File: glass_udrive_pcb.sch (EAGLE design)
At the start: 23 parts

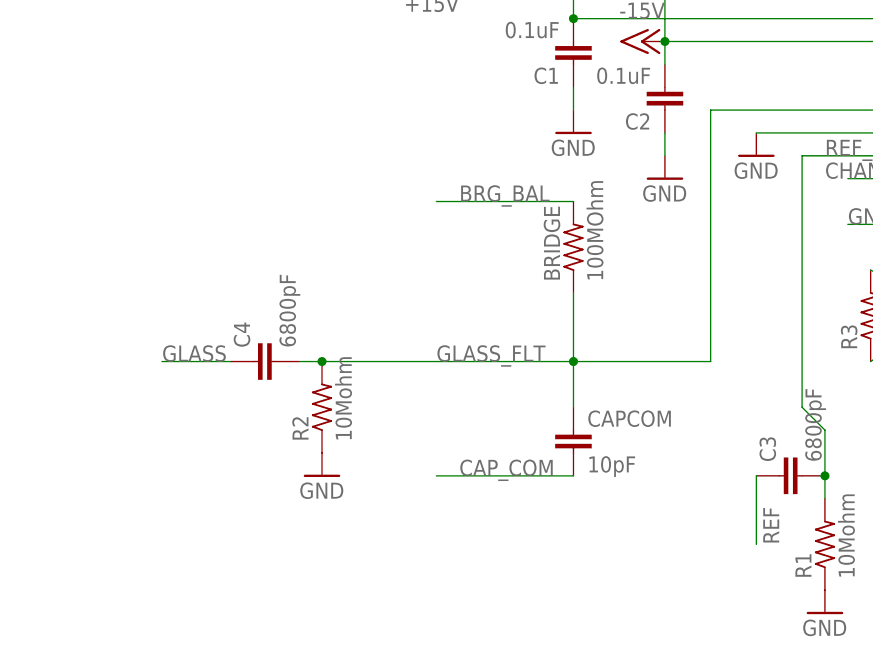
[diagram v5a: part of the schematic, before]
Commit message: solved the order of CAPCOM and Bridge balance nets and routing as per GFL suggestions.
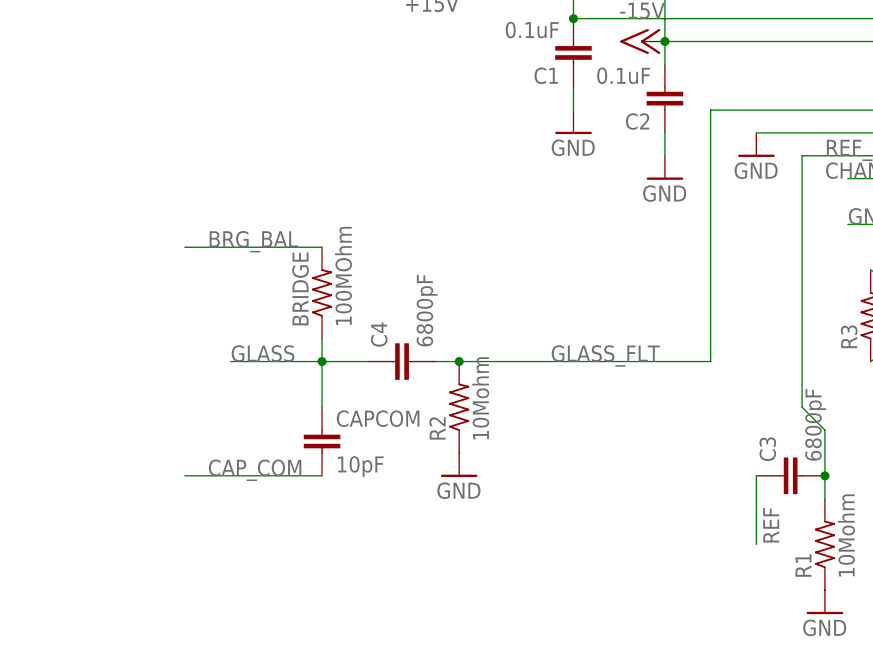
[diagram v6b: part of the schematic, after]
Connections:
- net GLASS: now also BRIDGE.1, CAPCOM.1
- net GLASS_FLT: no longer BRIDGE.1, CAPCOM.1
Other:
- moved on the sheet: BRIDGE, C4, CAPCOM, R2
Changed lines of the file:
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@@
 <instance part="FRAME1" gate="G$2" x="121.92" y="-10.16"/>
 <instance part="OMNETICS" gate="G$1" x="58.42" y="116.84"/>
-<instance part="BRIDGE" gate="R" x="116.84" y="71.12" rot="R90"/>
-<instance part="CAPCOM" gate="C" x="116.84" y="50.8"/>
+<instance part="BRIDGE" gate="R" x="88.9" y="66.04" rot="R90"/>
+<instance part="CAPCOM" gate="C" x="88.9" y="50.8"/>
 <instance part="C1" gate="C" x="116.84" y="91.44" rot="R180"/>
 <instance part="C2" gate="C" x="127" y="86.36" rot="R180"/>
@@
 <instance part="REF" gate="P" x="-5.08" y="15.24"/>
 <instance part="R3" gate="R" x="149.86" y="63.5" rot="R90"/>
-<instance part="R2" gate="R" x="88.9" y="53.34" rot="R90"/>
-<instance part="C4" gate="C" x="81.28" y="58.42" rot="R90"/>
+<instance part="R2" gate="R" x="104.14" y="53.34" rot="R90"/>
+<instance part="C4" gate="C" x="96.52" y="58.42" rot="R90"/>
 <instance part="GND3" gate="1" x="137.16" y="81.28"/>
-<instance part="GND4" gate="1" x="88.9" y="45.72"/>
+<instance part="GND4" gate="1" x="104.14" y="45.72"/>
 <instance part="R1" gate="R" x="144.78" y="38.1" rot="R90"/>
 <instance part="C3" gate="C" x="139.7" y="45.72" rot="R90"/>
@@
 <segment>
 <pinref part="CAPCOM" gate="C" pin="2"/>
-<wire x1="116.84" y1="45.72" x2="101.6" y2="45.72" width="0.1524" layer="91"/>
-<label x="104.14" y="45.72" size="1.778" layer="95"/>
+<wire x1="88.9" y1="45.72" x2="73.66" y2="45.72" width="0.1524" layer="91"/>
+<label x="76.2" y="45.72" size="1.778" layer="95"/>
 </segment>
 </net>
@@
 <segment>
 <pinref part="BRIDGE" gate="R" pin="2"/>
-<wire x1="116.84" y1="76.2" x2="101.6" y2="76.2" width="0.1524" layer="91"/>
-<label x="104.14" y="76.2" size="1.778" layer="95"/>
+<wire x1="88.9" y1="71.12" x2="73.66" y2="71.12" width="0.1524" layer="91"/>
+<label x="76.2" y="71.12" size="1.778" layer="95"/>
 </segment>
 </net>
@@
 <segment>
 <pinref part="C4" gate="C" pin="1"/>
-<wire x1="78.74" y1="58.42" x2="71.12" y2="58.42" width="0.1524" layer="91"/>
-<label x="71.12" y="58.42" size="1.778" layer="95"/>
+<wire x1="93.98" y1="58.42" x2="88.9" y2="58.42" width="0.1524" layer="91"/>
+<label x="78.74" y="58.42" size="1.778" layer="95"/>
+<pinref part="BRIDGE" gate="R" pin="1"/>
+<wire x1="88.9" y1="58.42" x2="78.74" y2="58.42" width="0.1524" layer="91"/>
+<wire x1="88.9" y1="60.96" x2="88.9" y2="58.42" width="0.1524" layer="91"/>
+<junction x="88.9" y="58.42"/>
+<pinref part="CAPCOM" gate="C" pin="1"/>
+<wire x1="88.9" y1="53.34" x2="88.9" y2="58.42" width="0.1524" layer="91"/>
 </segment>
 </net>
@@
 <net name="GLASS_FLT" class="0">
 <segment>
-<pinref part="CAPCOM" gate="C" pin="1"/>
-<wire x1="116.84" y1="53.34" x2="116.84" y2="58.42" width="0.1524" layer="91"/>
-<junction x="116.84" y="58.42"/>
-<pinref part="BRIDGE" gate="R" pin="1"/>
-<wire x1="116.84" y1="58.42" x2="116.84" y2="66.04" width="0.1524" layer="91"/>
-<wire x1="116.84" y1="58.42" x2="88.9" y2="58.42" width="0.1524" layer="91"/>
-<label x="101.6" y="58.42" size="1.778" layer="95"/>
-<wire x1="116.84" y1="58.42" x2="132.08" y2="58.42" width="0.1524" layer="91"/>
+<wire x1="132.08" y1="58.42" x2="104.14" y2="58.42" width="0.1524" layer="91"/>
+<label x="114.3" y="58.42" size="1.778" layer="95"/>
 <wire x1="132.08" y1="58.42" x2="132.08" y2="86.36" width="0.1524" layer="91"/>
 <pinref part="AD8224" gate="A" pin="+IN1"/>
 <wire x1="132.08" y1="86.36" x2="157.48" y2="86.36" width="0.1524" layer="91"/>
 <pinref part="R2" gate="R" pin="2"/>
-<wire x1="88.9" y1="58.42" x2="86.36" y2="58.42" width="0.1524" layer="91"/>
-<junction x="88.9" y="58.42"/>
+<wire x1="104.14" y1="58.42" x2="101.6" y2="58.42" width="0.1524" layer="91"/>
+<junction x="104.14" y="58.42"/>
 <pinref part="C4" gate="C" pin="2"/>
 </segment>
